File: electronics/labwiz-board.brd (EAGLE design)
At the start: 98.8 x 51.3 mm, 130 parts, among them IC1 MCP3424, J1 SD_MICRO_SDIO_1BIT, J2 CORTEX_DEBUGSMD, J30 4P-SMD-2.0-90D, J4 4P-SMD-2.0-90D, J5 4P-SMD-2.0-90D, U1 STM32F10XRXT6, U4 MIC5219-3.3V, X2 M12_BOTTOM_CONTACTS_FPC_1MM, Y1 32.768kHz, Y3 32.768kHz

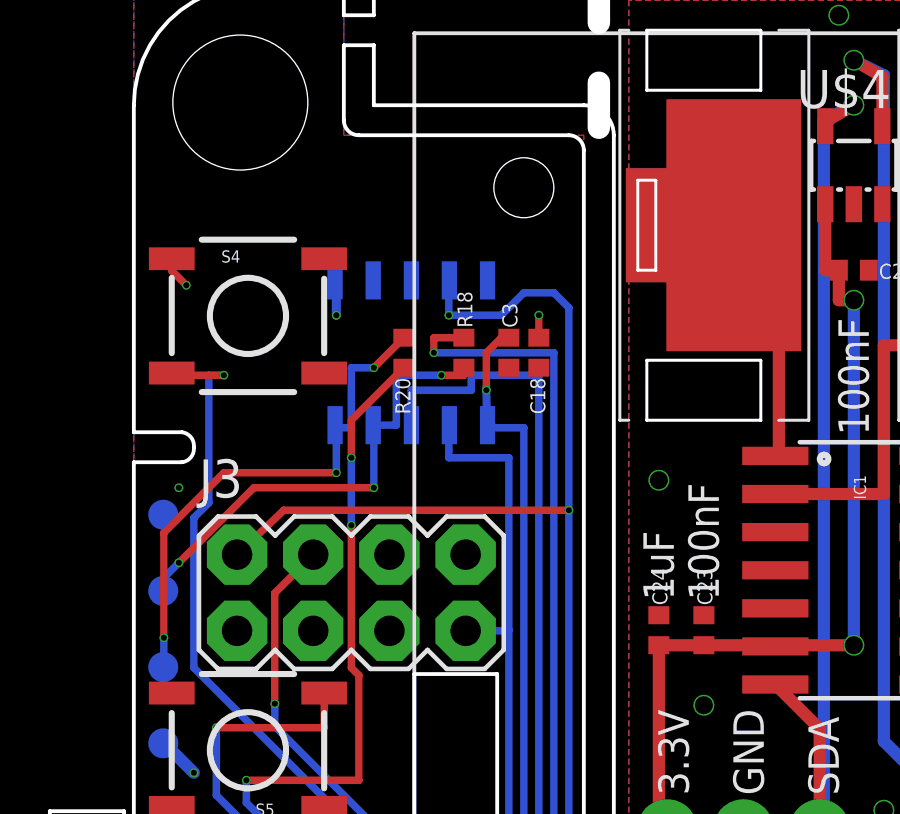
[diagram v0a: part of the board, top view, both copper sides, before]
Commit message: Added a header for USART1 Rx Tx.
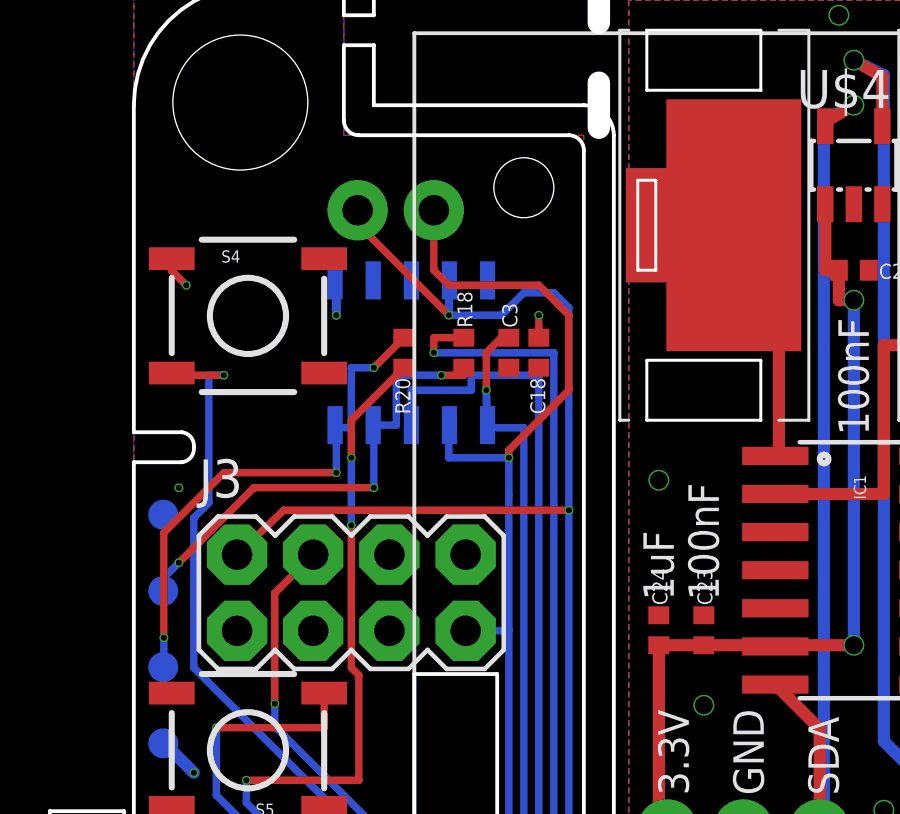
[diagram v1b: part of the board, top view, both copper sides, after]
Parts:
- added J43: (no value), SparkFun-Connectors:1X02
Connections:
- net USART1_RX: now also J43.2
- net USART1_TX: now also J43.1
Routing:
- net USART1_TX: track 47.1 -> 59.8 mm, vias 3 -> 4
- net USART1_RX: track 68.2 -> 74.1 mm
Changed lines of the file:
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@@
 <setting verticaltext="up"/>
 </settings>
-<grid distance="0.5" unitdist="mm" unit="mm" style="lines" multiple="1" display="yes" altdistance="0.05" altunitdist="mil" altunit="inch"/>
+<grid distance="0.25" unitdist="mm" unit="mm" style="lines" multiple="1" display="yes" altdistance="0.05" altunitdist="mil" altunit="inch"/>
 <layers>
 <layer number="1" name="Top" color="4" fill="1" visible="yes" active="yes"/>
@@
 <element name="J41" library="SparkFun-Connectors" package="PAD-1.5X4.5" value="" x="66" y="35"/>
 <element name="J42" library="SparkFun-Connectors" package="PAD-1.5X4.5" value="" x="66" y="29"/>
+<element name="J43" library="SparkFun-Connectors" package="1X02" value="" x="10" y="43.5" rot="MR0"/>
 </elements>
 <signals>
@@
 <via x="12.5" y="11.5" extent="1-16" drill="0.2"/>
 <wire x1="12.5" y1="11.5" x2="12.5" y2="29.5" width="0.25" layer="16"/>
-<wire x1="12.5" y1="29.5" x2="12.5" y2="35.25" width="0.25" layer="16"/>
+<wire x1="12.5" y1="29.5" x2="12.5" y2="34" width="0.25" layer="16"/>
 <wire x1="12.5" y1="35.25" x2="10.5" y2="35.25" width="0.25" layer="16"/>
 <wire x1="10.5" y1="35.25" x2="10.5" y2="35.5" width="0.25" layer="16"/>
@@
 <wire x1="11.06" y1="29.48" x2="12.48" y2="29.48" width="0.25" layer="16"/>
 <wire x1="12.48" y1="29.48" x2="12.5" y2="29.5" width="0.25" layer="16"/>
+<contactref element="J43" pad="1"/>
+<wire x1="10" y1="43.5" x2="10" y2="41.5" width="0.25" layer="1"/>
+<wire x1="10" y1="41.5" x2="10.5" y2="41" width="0.25" layer="1"/>
+<wire x1="10.5" y1="41" x2="13.5" y2="41" width="0.25" layer="1"/>
+<wire x1="13.5" y1="41" x2="14.5" y2="40" width="0.25" layer="1"/>
+<wire x1="14.5" y1="40" x2="14.5" y2="37.5" width="0.25" layer="1"/>
+<wire x1="14.5" y1="37.5" x2="12.5" y2="35.5" width="0.25" layer="1"/>
+<wire x1="12.5" y1="35.5" x2="12.5" y2="35.25" width="0.25" layer="1"/>
+<via x="12.5" y="35.25" extent="1-16" drill="0.2" shape="square"/>
+<wire x1="12.5" y1="35.25" x2="12.5" y2="34" width="0.25" layer="16"/>
 </signal>
 <signal name="USART1_RX">
@@
 <wire x1="12.25" y1="40" x2="10.5" y2="40" width="0.25" layer="16"/>
 <contactref element="J3" pad="2"/>
-<via x="10.5" y="40" extent="1-16" drill="0.2"/>
 <wire x1="3.44" y1="32.02" x2="3.5" y2="32.08" width="0.25" layer="1"/>
 <wire x1="3.5" y1="32.08" x2="5" y2="33.5" width="0.25" layer="1"/>
 <wire x1="5" y1="33.5" x2="14.5" y2="33.5" width="0.25" layer="1"/>
 <via x="14.5" y="33.5" extent="1-16" drill="0.2"/>
+<contactref element="J43" pad="2"/>
+<wire x1="10.52" y1="41.163" x2="10.52" y2="40.02" width="0.25" layer="16"/>
+<wire x1="10.52" y1="40.02" x2="10.5" y2="40" width="0.25" layer="16"/>
+<via x="10.5" y="40" extent="1-16" drill="0.2" shape="square"/>
+<wire x1="10.5" y1="40" x2="7.5" y2="43" width="0.25" layer="1"/>
+<wire x1="7.5" y1="43" x2="7.5" y2="43.46" width="0.25" layer="1"/>
+<wire x1="7.5" y1="43.46" x2="7.46" y2="43.5" width="0.25" layer="1"/>
 </signal>
 <signal name="SWDIO_M">

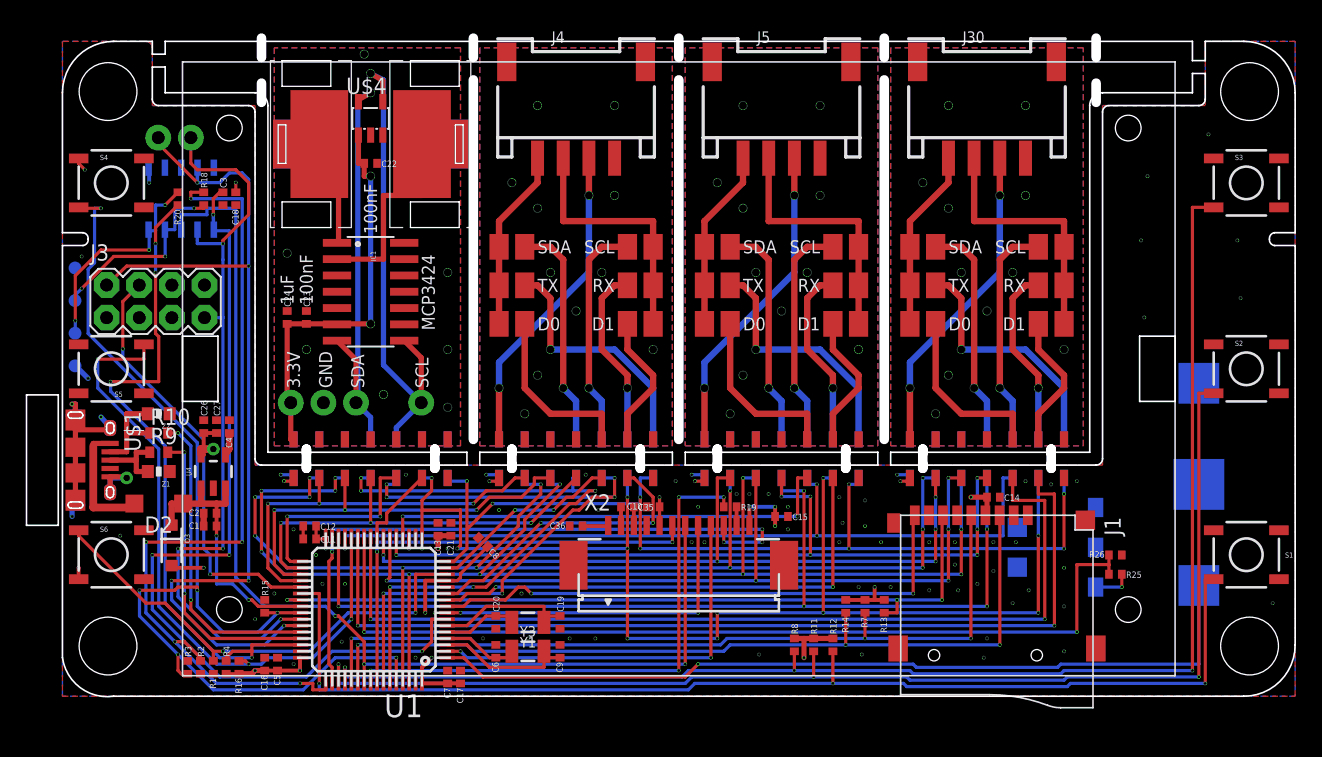
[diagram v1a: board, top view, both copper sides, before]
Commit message: Added pin docs to silk.
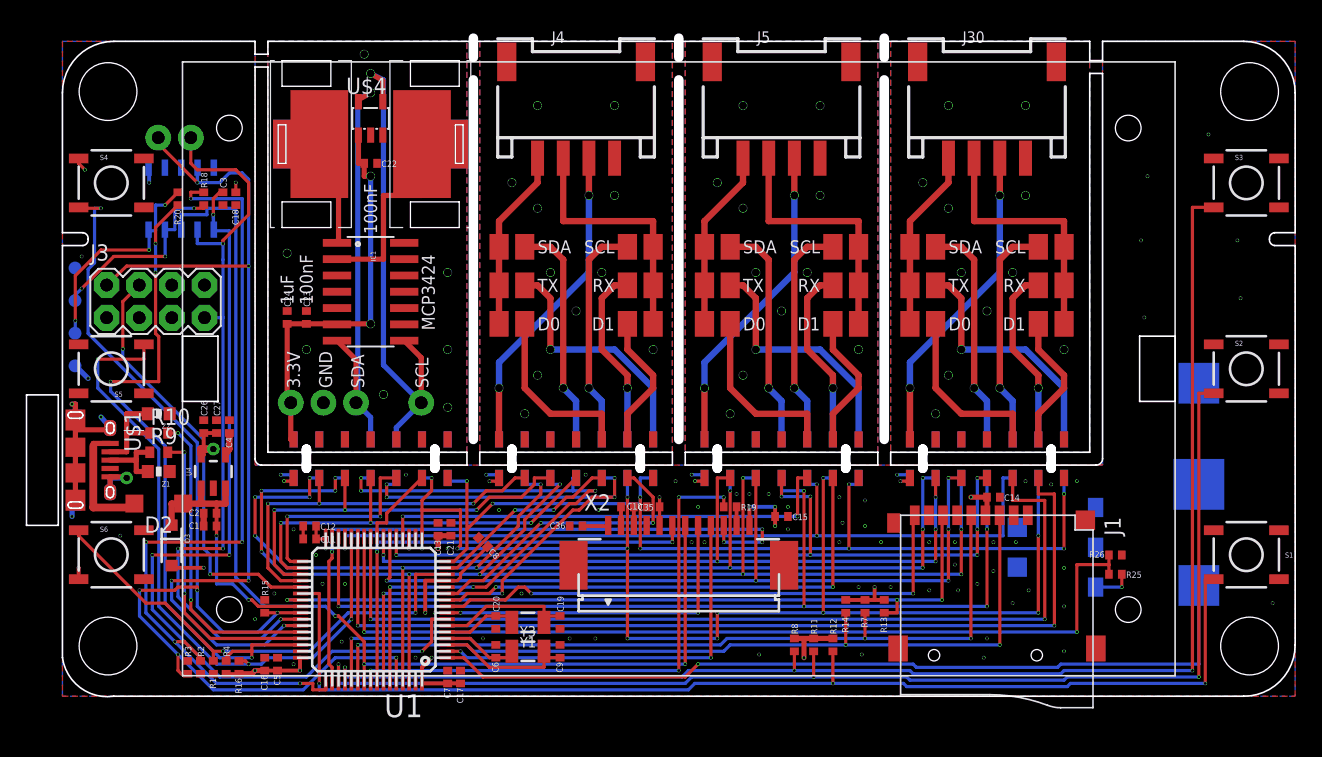
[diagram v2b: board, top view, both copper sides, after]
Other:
- outline, holes or cut-outs redrawn
- board text added: "CORTEX"
- board text added: "ESP8266"
- board text added: "SWDCLK"
- board text added: "SWDIO"
- board text added: "USART1"

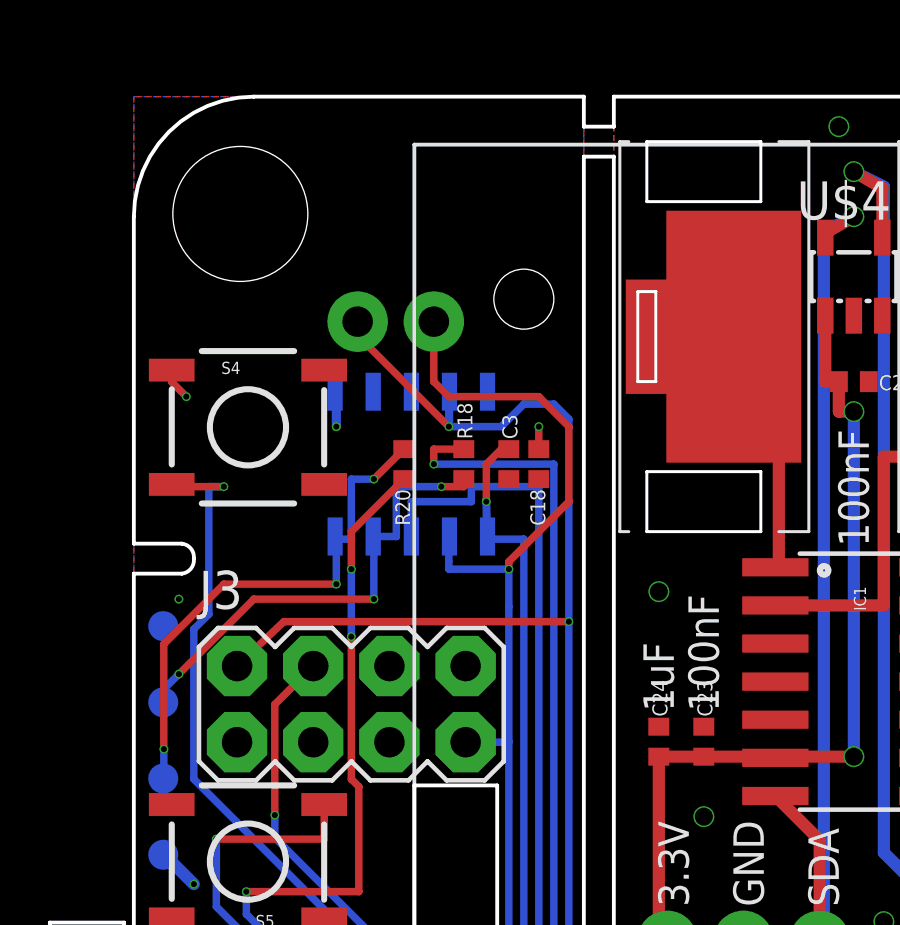
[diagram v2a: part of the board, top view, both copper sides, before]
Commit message: Moved USART1. Added USART1 pullup resistors.
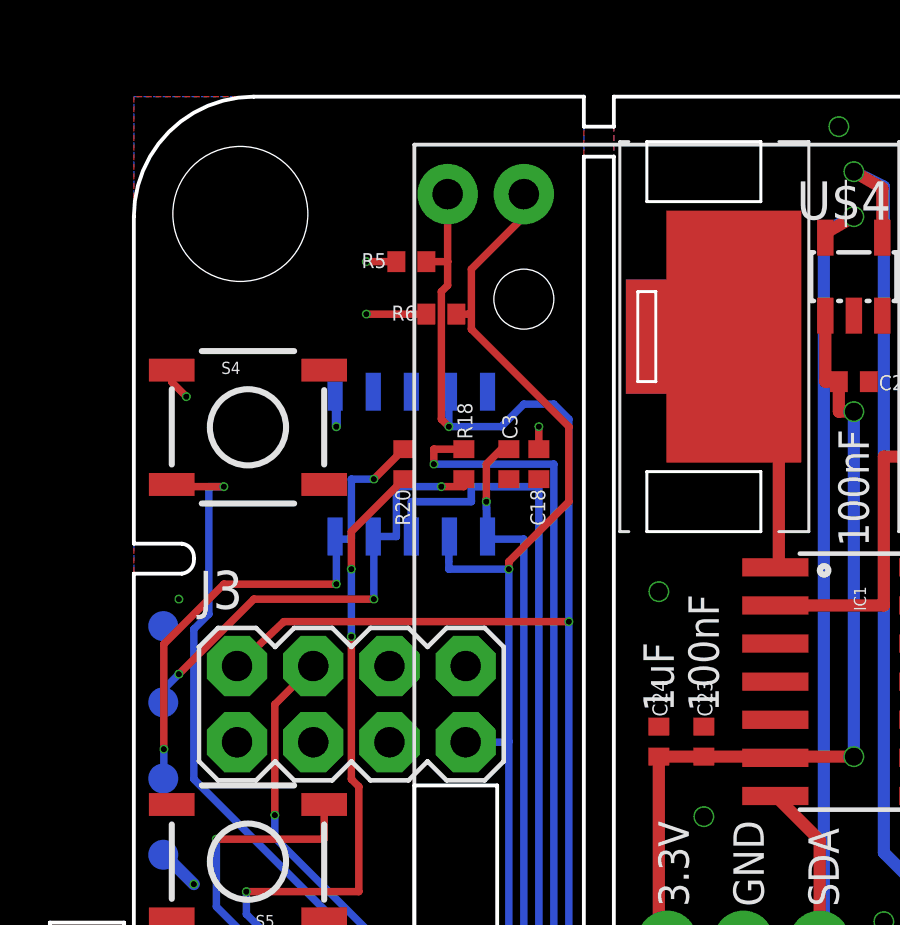
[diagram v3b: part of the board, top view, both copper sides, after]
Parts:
- added R5, R6: 100K, PaxInstruments-RCL:0402
- moved J43 5.20 mm to (13.0, 47.8)
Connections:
- net 3.3V: now also R5.1, R6.1
- net USART1_RX: now also R5.2
- net USART1_TX: now also R6.2
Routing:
- net USART1_TX: track 59.8 -> 63.0 mm
- net 3.3V: track 61.9 -> 64.9 mm, vias 25 -> 27
- net USART1_RX: track 74.1 -> 77.0 mm
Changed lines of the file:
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@@
 <layer number="19" name="Unrouted" color="6" fill="1" visible="yes" active="yes"/>
 <layer number="20" name="Dimension" color="13" fill="1" visible="yes" active="yes"/>
-<layer number="21" name="tPlace" color="7" fill="1" visible="no" active="yes"/>
+<layer number="21" name="tPlace" color="7" fill="1" visible="yes" active="yes"/>
 <layer number="22" name="bPlace" color="14" fill="1" visible="yes" active="yes"/>
-<layer number="23" name="tOrigins" color="15" fill="1" visible="no" active="yes"/>
+<layer number="23" name="tOrigins" color="15" fill="1" visible="yes" active="yes"/>
 <layer number="24" name="bOrigins" color="15" fill="1" visible="yes" active="yes"/>
 <layer number="25" name="tNames" color="7" fill="1" visible="no" active="yes"/>
@@
 <layer number="49" name="Reference" color="7" fill="1" visible="yes" active="yes"/>
 <layer number="50" name="dxf" color="7" fill="1" visible="no" active="no"/>
-<layer number="51" name="tDocu" color="6" fill="1" visible="no" active="yes"/>
+<layer number="51" name="tDocu" color="6" fill="1" visible="yes" active="yes"/>
 <layer number="52" name="bDocu" color="7" fill="1" visible="yes" active="yes"/>
 <layer number="53" name="tGND_GNDA" color="7" fill="9" visible="no" active="no"/>
@@
 <wire x1="1.75" y1="25" x2="1.75" y2="23.5" width="0.2" layer="22"/>
 <wire x1="1.75" y1="33.75" x2="1.25" y2="34.25" width="0.2" layer="22"/>
-<text x="12" y="46.75" size="1" layer="22" rot="MR0">USART1</text>
-<text x="11" y="45.25" size="1" layer="22" rot="MR0">TX</text>
-<text x="8.5" y="45.25" size="1" layer="22" rot="MR0">RX</text>
+<text x="7.5" y="45" size="1" layer="22" rot="MR90">USART1</text>
+<text x="14" y="49.5" size="1" layer="22" rot="MR0">TX</text>
+<text x="11.25" y="49.5" size="1" layer="22" rot="MR0">RX</text>
 <text x="5.5" y="41.25" size="1" layer="22" rot="MR270">CORTEX</text>
 <text x="9.5" y="33.75" size="1" layer="22" rot="MR0">ESP8266</text>
@@
 <element name="J41" library="SparkFun-Connectors" package="PAD-1.5X4.5" value="" x="66" y="35"/>
 <element name="J42" library="SparkFun-Connectors" package="PAD-1.5X4.5" value="" x="66" y="29"/>
-<element name="J43" library="SparkFun-Connectors" package="1X02" value="" x="10" y="43.5" rot="MR0"/>
+<element name="J43" library="SparkFun-Connectors" package="1X02" value="" x="13" y="47.75" rot="MR0"/>
+<element name="R5" library="PaxInstruments-RCL" package="0402" value="100K" x="9.25" y="45.5">
+<attribute name="MPN" value="" x="9.25" y="45.5" size="1" layer="27" display="off"/>
+<attribute name="POPULATE" value="" x="9.25" y="45.5" size="1" layer="27" display="off"/>
+</element>
+<element name="R6" library="PaxInstruments-RCL" package="0402" value="100K" x="10.25" y="43.75">
+<attribute name="MPN" value="" x="10.25" y="43.75" size="1" layer="27" display="off"/>
+<attribute name="POPULATE" value="" x="10.25" y="43.75" size="1" layer="27" display="off"/>
+</element>
 </elements>
 <signals>
@@
 <wire x1="0.98" y1="25.73" x2="1.02" y2="25.73" width="0.4064" layer="16"/>
 <wire x1="1.02" y1="25.73" x2="2" y2="24.75" width="0.4064" layer="16"/>
+<contactref element="R5" pad="1"/>
+<contactref element="R6" pad="1"/>
+<via x="7.75" y="45.5" extent="1-16" drill="0.2"/>
+<via x="7.75" y="43.75" extent="1-16" drill="0.2"/>
+<wire x1="8.75" y1="45.5" x2="7.75" y2="45.5" width="0.25" layer="1"/>
+<wire x1="9.75" y1="43.75" x2="7.75" y2="43.75" width="0.25" layer="1"/>
 </signal>
 <signal name="GND" class="5">
@@
 <via x="12.5" y="11.5" extent="1-16" drill="0.2"/>
 <wire x1="12.5" y1="11.5" x2="12.5" y2="29.5" width="0.25" layer="16"/>
-<wire x1="12.5" y1="29.5" x2="12.5" y2="34" width="0.25" layer="16"/>
+<wire x1="12.5" y1="29.5" x2="12.5" y2="35.25" width="0.25" layer="16"/>
 <wire x1="12.5" y1="35.25" x2="10.5" y2="35.25" width="0.25" layer="16"/>
 <wire x1="10.5" y1="35.25" x2="10.5" y2="35.5" width="0.25" layer="16"/>
@@
 <wire x1="12.48" y1="29.48" x2="12.5" y2="29.5" width="0.25" layer="16"/>
 <contactref element="J43" pad="1"/>
-<wire x1="10" y1="43.5" x2="10" y2="41.5" width="0.25" layer="1"/>
-<wire x1="10" y1="41.5" x2="10.5" y2="41" width="0.25" layer="1"/>
-<wire x1="10.5" y1="41" x2="13.5" y2="41" width="0.25" layer="1"/>
-<wire x1="13.5" y1="41" x2="14.5" y2="40" width="0.25" layer="1"/>
 <wire x1="14.5" y1="40" x2="14.5" y2="37.5" width="0.25" layer="1"/>
 <wire x1="14.5" y1="37.5" x2="12.5" y2="35.5" width="0.25" layer="1"/>
 <wire x1="12.5" y1="35.5" x2="12.5" y2="35.25" width="0.25" layer="1"/>
 <via x="12.5" y="35.25" extent="1-16" drill="0.2" shape="square"/>
-<wire x1="12.5" y1="35.25" x2="12.5" y2="34" width="0.25" layer="16"/>
+<wire x1="14.5" y1="40" x2="11.25" y2="43.25" width="0.25" layer="1"/>
+<wire x1="11.25" y1="43.25" x2="11.25" y2="43.75" width="0.25" layer="1"/>
+<wire x1="11.25" y1="43.75" x2="11.25" y2="45.25" width="0.25" layer="1"/>
+<wire x1="11.25" y1="45.25" x2="13" y2="47" width="0.25" layer="1"/>
+<wire x1="13" y1="47" x2="13" y2="47.75" width="0.25" layer="1"/>
+<contactref element="R6" pad="2"/>
+<wire x1="10.75" y1="43.75" x2="11.25" y2="43.75" width="0.25" layer="1"/>
 </signal>
 <signal name="USART1_RX">
@@
 <via x="17.25" y="5.5" extent="1-16" drill="0.2"/>
 <contactref element="J2" pad="7"/>
-<wire x1="10.5" y1="40" x2="10.5" y2="41.143" width="0.254" layer="16"/>
 <wire x1="10.5" y1="41.143" x2="10.52" y2="41.163" width="0.254" layer="16"/>
 <wire x1="8.5" y1="7.5" x2="8.5" y2="9" width="0.25" layer="16"/>
@@
 <via x="14.5" y="33.5" extent="1-16" drill="0.2"/>
 <contactref element="J43" pad="2"/>
-<wire x1="10.52" y1="41.163" x2="10.52" y2="40.02" width="0.25" layer="16"/>
 <wire x1="10.52" y1="40.02" x2="10.5" y2="40" width="0.25" layer="16"/>
 <via x="10.5" y="40" extent="1-16" drill="0.2" shape="square"/>
-<wire x1="10.5" y1="40" x2="7.5" y2="43" width="0.25" layer="1"/>
-<wire x1="7.5" y1="43" x2="7.5" y2="43.46" width="0.25" layer="1"/>
-<wire x1="7.5" y1="43.46" x2="7.46" y2="43.5" width="0.25" layer="1"/>
+<contactref element="R5" pad="2"/>
+<wire x1="10.46" y1="45.5" x2="10.46" y2="47.75" width="0.25" layer="1"/>
+<wire x1="9.75" y1="45.5" x2="10.46" y2="45.5" width="0.25" layer="1"/>
+<wire x1="10.25" y1="40.25" x2="10.25" y2="44.5" width="0.25" layer="1"/>
+<wire x1="10.25" y1="44.5" x2="10.46" y2="44.71" width="0.25" layer="1"/>
+<wire x1="10.46" y1="44.71" x2="10.46" y2="45.5" width="0.25" layer="1"/>
+<wire x1="10.52" y1="40.02" x2="10.5" y2="40.04" width="0.25" layer="16"/>
+<wire x1="10.5" y1="40.04" x2="10.46" y2="40.04" width="0.25" layer="16"/>
+<wire x1="10.25" y1="40.25" x2="10.5" y2="40" width="0.25" layer="1"/>
+<wire x1="10.5" y1="41.143" x2="10.5" y2="40" width="0.25" layer="16"/>
 </signal>
 <signal name="SWDIO_M">
@@
 <vertex x="63.5" y="51"/>
 </polygon>
+<via x="53" y="46" extent="1-16" drill="0.6" shape="square"/>
+<via x="59" y="46" extent="1-16" drill="0.6" shape="square"/>
 </signal>
 <signal name="3.3V_4">
@@
 <vertex x="80" y="51"/>
 </polygon>
-</signal>
-<signal name="GND_5" class="5">
-<via x="53" y="46" extent="1-16" drill="0.6" shape="square"/>
-<via x="59" y="46" extent="1-16" drill="0.6" shape="square"/>
-</signal>
-<signal name="GND_6" class="5">
 <via x="69" y="46" extent="1-16" drill="0.6" shape="square"/>
 <via x="75" y="46" extent="1-16" drill="0.6" shape="square"/>
